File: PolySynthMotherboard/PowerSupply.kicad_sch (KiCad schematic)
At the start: 44 parts, among them J502 BATTERY, J503 POWER, Q501 Q_PMOS_GSD, Q502 Q_PMOS_GSD, U501 MAX1898, U502 TPS61200DRC, U503 CS5173, U702 TC7662Bx0A, U705 TC7662Bx0A

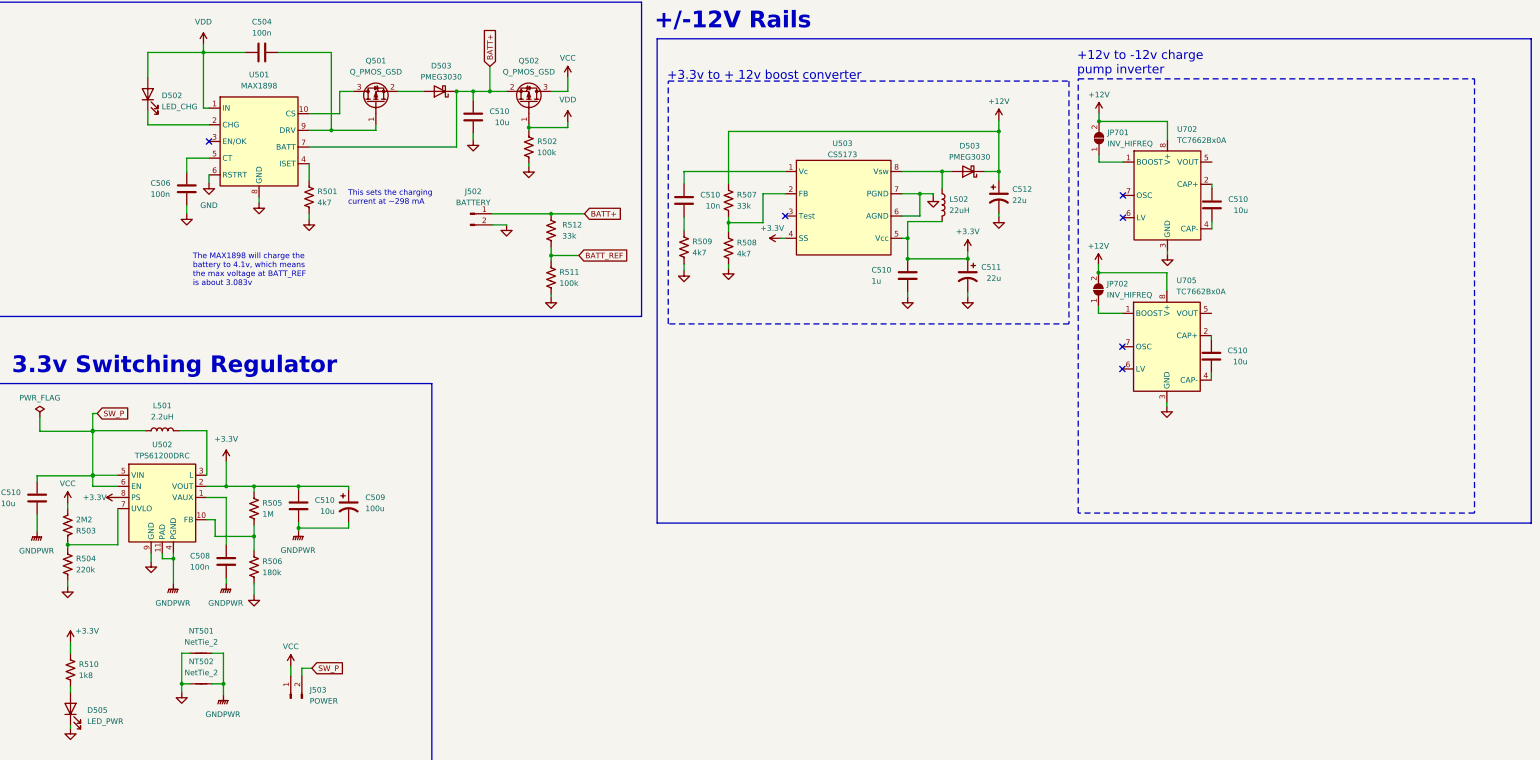
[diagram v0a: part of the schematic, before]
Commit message: net class assignment
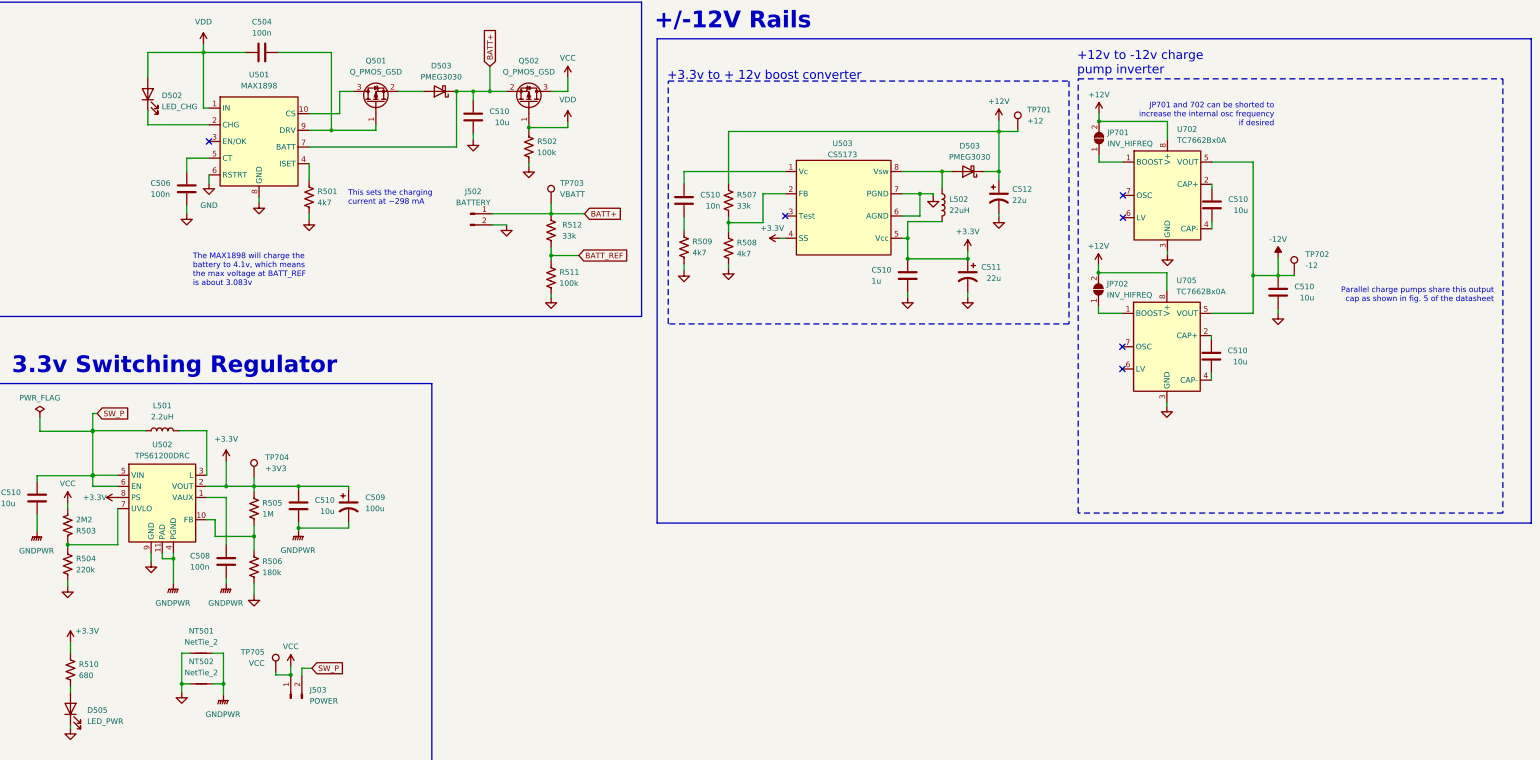
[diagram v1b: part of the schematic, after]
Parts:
- added C510: 10u, Capacitor_SMD:C_0805_2012Metric, symbol Device:C
- added TP701: +12, TestPoint:TestPoint_Pad_D1.0mm_Value, symbol Connector:TestPoint
- added TP702: -12, TestPoint:TestPoint_Pad_D1.0mm_Value, symbol Connector:TestPoint
- added TP703: VBATT, TestPoint:TestPoint_Pad_D1.0mm_Value, symbol Connector:TestPoint
- added TP704: +3V3, TestPoint:TestPoint_Pad_D1.0mm_Value, symbol Connector:TestPoint
- added TP705: VCC, TestPoint:TestPoint_Pad_D1.0mm_Value, symbol Connector:TestPoint
- JP701, JP702: footprint (none) -> Jumper:SolderJumper-2_Open_TrianglePad_0805
- R510: value 1k8 -> 680
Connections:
- net +12V: now also TP701.1
- net +3.3V: now also TP704.1
- net BATT+: now also TP703.1
- net GND: now also C510.2
- net VCC: now also TP705.1
- net -12V: now reaches U705.5 (VOUT)
- net -12V: now also U702.5 (VOUT), C510.1, TP702.1
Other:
- note added: "JP701 and 702 can be shorted to increase the internal osc frequency if desired"
- note added: "Parallel charge pumps share this output cap as shown in fig. 5 of the datasheet"

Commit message: board layout
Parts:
- U503: footprint PCM_4ms_Package_SOIC:SOIC-8_5.28x4.9mm_Pitch1.27mm -> Package_SO:SOIC-8_3.9x4.9mm_P1.27mm
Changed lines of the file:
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@@
       (effects (font (size 1.27 1.27)))
     )
-    (property "Footprint" "PCM_4ms_Package_SOIC:SOIC-8_5.28x4.9mm_Pitch1.27mm" (at 216.535 86.106 0)
+    (property "Footprint" "Package_SO:SOIC-8_3.9x4.9mm_P1.27mm" (at 216.535 86.106 0)
       (effects (font (size 1.27 1.27)) hide)
     )

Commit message: new voice board proj
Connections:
- net BATT_REF renamed BATT_LEF
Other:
- note added: "The MAX1898 will charge the battery to 4.1v, which means the max voltage at BATT_LEF is about 3.083v"
- note removed: "The MAX1898 will charge the battery to 4.1v, which means the max voltage at BATT_REF is about 3.083v"
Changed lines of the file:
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@@
     (effects (font (size 3.81 3.81) (thickness 0.762) bold) (justify left bottom))
   )
-  (text "The MAX1898 will charge the\nbattery to 4.1v, which means \nthe max voltage at BATT_REF \nis about 3.083v"
+  (text "The MAX1898 will charge the\nbattery to 4.1v, which means \nthe max voltage at BATT_LEF \nis about 3.083v"
     (at 69.85 104.8004 0)
     (effects (font (size 1.27 1.27)) (justify left bottom))
@@
     )
   )
-  (global_label "BATT_REF" (shape input) (at 157.988 97.663 0) (fields_autoplaced)
+  (global_label "BATT_LEF" (shape input) (at 157.988 97.663 0) (fields_autoplaced)
     (effects (font (size 1.27 1.27)) (justify left))
     (property "Intersheetrefs" "${INTERSHEET_REFS}" (at 169.7422 97.663 0)

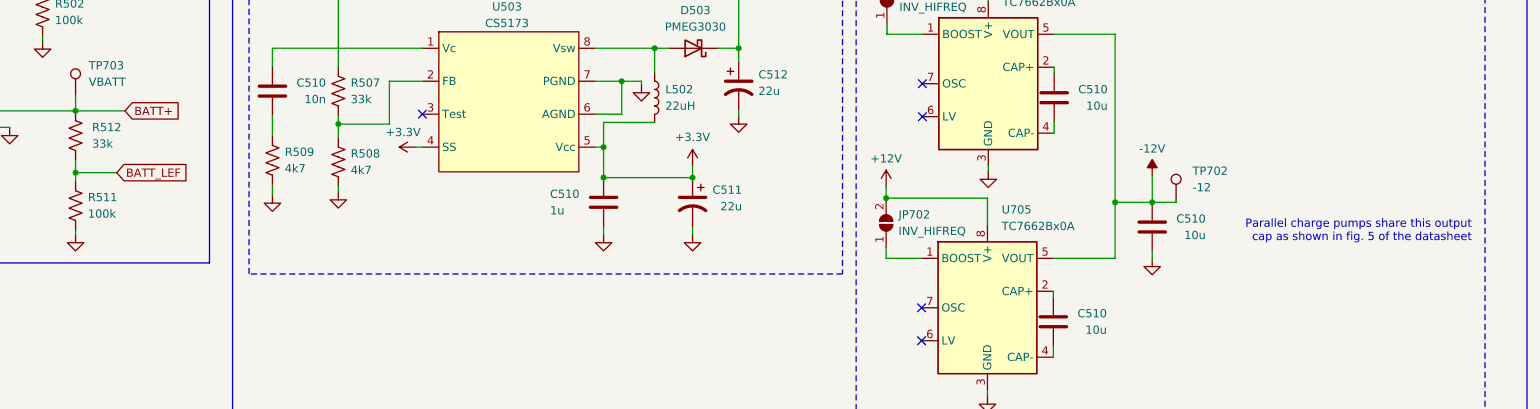
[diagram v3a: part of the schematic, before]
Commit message: op-amp layout improved
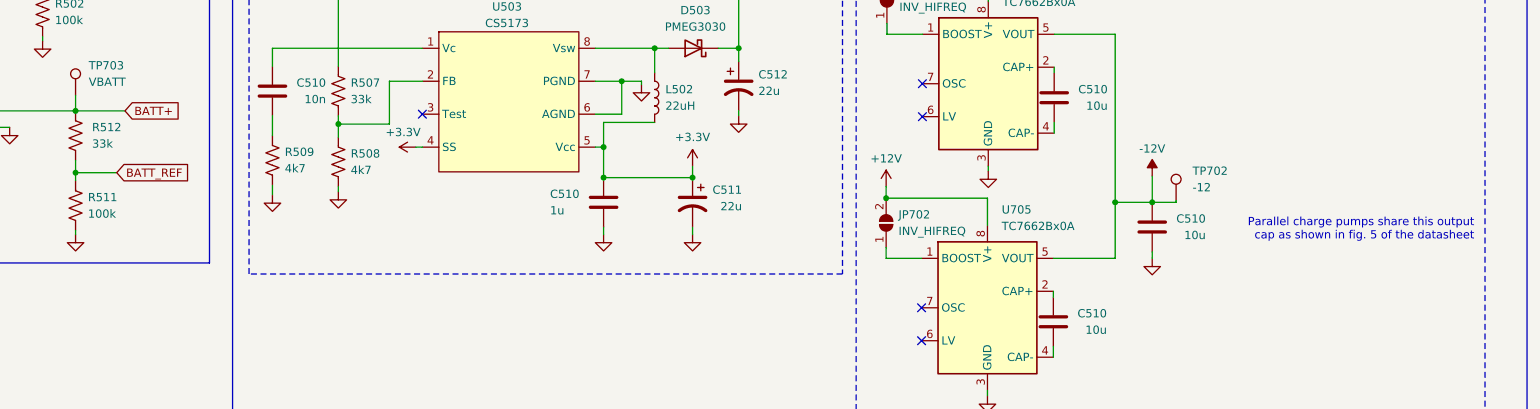
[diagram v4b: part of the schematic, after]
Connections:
- net BATT_LEF renamed BATT_REF
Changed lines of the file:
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@@
   )
   (text "Parallel charge pumps share this output\ncap as shown in fig. 5 of the datasheet"
-    (at 366.903 108.458 0)
+    (at 367.284 108.204 0)
     (effects (font (size 1.27 1.27)) (justify right bottom))
   )
@@
     )
   )
-  (global_label "BATT_LEF" (shape input) (at 157.988 97.663 0) (fields_autoplaced)
+  (global_label "BATT_REF" (shape input) (at 157.988 97.663 0) (fields_autoplaced)
     (effects (font (size 1.27 1.27)) (justify left))
     (property "Intersheetrefs" "${INTERSHEET_REFS}" (at 169.7422 97.663 0)

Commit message: power supply tweaks
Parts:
- removed C504, C506: 100n, Capacitor_SMD:C_0805_2012Metric, symbol Device:C
- removed C510: 10u, Capacitor_SMD:C_0805_2012Metric, symbol Device:C
- removed D502: LED_CHG, LED_THT:LED_D3.0mm, symbol Device:LED
- removed D503: PMEG3030, PCM_Diode_SMD_AKL:D_SOD-123, symbol Device:D_Schottky
- removed D505: LED_PWR, LED_THT:LED_D3.0mm, symbol Device:LED
- removed Q501, Q502: Q_PMOS_GSD, PCM_4ms_Package_SOT:SOT-23, symbol Device:Q_PMOS_GSD
- removed R501: 4k7, PCM_Resistor_SMD_AKL:R_0805_2012Metric, symbol Device:R_US
- removed R502: 100k, PCM_Resistor_SMD_AKL:R_0805_2012Metric, symbol Device:R_US
- removed R510: 680, PCM_Resistor_SMD_AKL:R_0805_2012Metric, symbol Device:R_US
- removed U501: MAX1898, PCM_Package_SO_AKL:MSOP-10_3x3mm_P0.5mm, symbol Battery_Management:MAX1898
- added C706: 2u2, symbol Device:C
- added C707: 10u, symbol Device:C
- added C708: 1u, symbol Device:C
- added D503 (x2): PMEG3030, PCM_Diode_SMD_AKL:D_SOD-123, symbol Device:D_Schottky
- added D702: PWR, symbol Device:LED
- added D703: CHG, symbol Device:LED
- added Q701: BSH205G2A, Package_TO_SOT_SMD_AKL:SOT-23, symbol Device:Q_PMOS_GSD
- added R704: 3k3, symbol Device:R_US
- added R705, R713: 470, symbol Device:R_US
- added R714: 10k, symbol Device:R_US
- added TH701: 10k, Resistor_SMD:R_0603_1608Metric, symbol Device:Thermistor_US
- added U703: MCP73834T, symbol Battery_Management:MCP73834T
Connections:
- net +3.3V: now also R705.1, R713.1, U703.7 (TE)
- net GND: now also C706.2, C707.2, C708.2, R704.2, R714.2, TH701.2, U703.5 (VSS)
- net VCC: now also C708.1, D503.1 (K), D503.1 (K)
- net VDD: now also C706.1, D503.2 (A), Q701.1 (G), R714.1, U703.1 (VDD), U703.2 (VDD)
- net BATT+ renamed VBATT
- net VBATT: now also C707.1, Q701.2 (S), U703.10 (VBATT), U703.9 (VBATT)
- new net: R704.1, U703.6 (PROG)
- new net: D702.2 (A), R713.2
- new net: D503.2 (A), Q701.3 (D)
- new net: D703.1 (K), U703.3 (STAT1)
- new net: D702.1 (K), U703.4 (STAT2)
- new net: TH701.1, U703.8 (THERM)
- new net: D703.2 (A), R705.2
- no-connect marks 6 -> 5
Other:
- note added: "Parallel charge pumps share output cap C713 as shown in fig. 5 of the datasheet"
- note added: "R704 sets the constant charging current at ~300mA (p. 14 of the datasheet)"
- note added: "This switches U704's input between the battery and the USB connector as appropriate"
- note removed: "Parallel charge pumps share this output cap as shown in fig. 5 of the datasheet"
- note removed: "The MAX1898 will charge the battery to 4.1v, which means the max voltage at BATT_LEF is about 3.083v"
- note removed: "This sets the charging current at ~298 mA"
- moved on the sheet: C508, C509, C510, J502, J503, JP701, JP702, L501, NT501, NT502, R503, R504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

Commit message: fixed git maybe
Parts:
- removed C508: 100n, Capacitor_SMD:C_0805_2012Metric, symbol Device:C
- removed C509: 100u, Capacitor_THT:CP_Radial_D5.0mm_P2.00mm, symbol Device:C_Polarized_US
- removed C510 (x2): 10u, Capacitor_SMD:C_0805_2012Metric, symbol Device:C
- removed J503: POWER, Connector_PinHeader_2.54mm:PinHeader_1x02_P2.54mm_Vertical, symbol Connector:Conn_01x02_Pin
- removed L501: 2.2uH, Inductor_SMD:L_Changjiang_FNR4010S, symbol Device:L
- removed NT501, NT502: NetTie_2, NetTie:NetTie-2_SMD_Pad0.5mm, symbol Device:NetTie_2
- removed R503: 2M2, PCM_Resistor_SMD_AKL:R_0805_2012Metric, symbol Device:R_US
- removed R504: 220k, PCM_Resistor_SMD_AKL:R_0805_2012Metric, symbol Device:R_US
- removed R505: 1M, PCM_Resistor_SMD_AKL:R_0805_2012Metric, symbol Device:R_US
- removed R506: 180k, PCM_Resistor_SMD_AKL:R_0805_2012Metric, symbol Device:R_US
- removed TP704: +3V3, TestPoint:TestPoint_Pad_D1.0mm_Value, symbol Connector:TestPoint
- removed TP705: VCC, TestPoint:TestPoint_Pad_D1.0mm_Value, symbol Connector:TestPoint
- removed U502: TPS61200DRC, Package_SON:VSON-10-1EP_3x3mm_P0.5mm_EP1.2x2mm, symbol Regulator_Switching:TPS61200DRC
- added C510 (x2): 1u, Capacitor_SMD:C_0805_2012Metric, symbol Device:C
- added C510, C712: 22u, Capacitor_SMD:C_0805_2012Metric, symbol Device:C
- added C510 (x3), C711: 100n, Capacitor_SMD:C_0805_2012Metric, symbol Device:C
- added C709, C710: 10u, Capacitor_SMD:C_0805_2012Metric, symbol Device:C
- added D704: LED, LED_SMD:LED_0805_2012Metric, symbol Device:LED
- added J502: POWER, Connector_PinHeader_2.54mm:PinHeader_1x02_P2.54mm_Vertical, symbol Connector:Conn_01x02_Pin
- added JP703: POS_CM, Jumper:SolderJumper-2_Open_TrianglePad_0805, symbol Jumper:SolderJumper_2_Open
- added JP704: NEG_CM, Jumper:SolderJumper-2_Open_TrianglePad_0805, symbol Jumper:SolderJumper_2_Open
- added JP705: DIG_CM, Jumper:SolderJumper-2_Open_TrianglePad_0805, symbol Jumper:SolderJumper_2_Open
- added L702: 1u5, Inductor_SMD:L_Coilcraft_XAL4020-XXX, symbol Device:L
- added Q702, Q703, Q704: TD6790, PCM_4ms_Package_SOIC:SM-8, symbol Transistor_BJT:TD6790
- added R511: 680, PCM_Resistor_SMD_AKL:R_0805_2012Metric, symbol Device:R_US
- added R709, R710, R715: 12k, PCM_Resistor_SMD_AKL:R_0805_2012Metric, symbol Device:R_US
- added U704: TPS63021, Package_SON:Texas_S-PVSON-N14, symbol Regulator_Switching:TPS63021
- C706, C707, C708: footprint (none) -> Capacitor_SMD:C_0805_2012Metric
- D702, D703: footprint (none) -> LED_THT:LED_D3.0mm
- Q701: footprint Package_TO_SOT_SMD_AKL:SOT-23 -> PCM_4ms_Package_SOT:SOT-23
- R704, R705, R713, R714: footprint (none) -> PCM_Resistor_SMD_AKL:R_0805_2012Metric
- TP701: value +12 -> +12A
- TP702: value -12 -> -12A
- U703: footprint (none) -> PCM_Package_SO_AKL:MSOP-10_3x3mm_P0.5mm
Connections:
- net +12V: now also C510.1, JP703.1 (A), Q703.3 (C2), Q703.7 (E1); no longer C512.1, D503.1 (K), R507.1, TP701.1
- net +3.3V: now also C510.1, JP705.1 (A), Q704.3 (C2), Q704.7 (E1)
- net -12V: now also C510.1, JP704.1 (A), Q702.1 (C1), Q702.5 (E2); no longer C510.1, TP702.1, U702.5 (VOUT), U705.5 (VOUT)
- net GND: now also C510.2, C510.2, C510.2, C510.2, C510.2, C510.2, C709.2, C710.2, C711.2, C712.2, U704.15 (PGND), U704.2 (GND)
- net VCC: now also J502.1 (Pin_1)
- new net: Q702.3 (C2), Q702.8 (B1)
- new net: C510.1, Q702.6 (B2), R715.2
- new net: Q704.1 (C1), Q704.6 (B2)
- new net: C510.1, Q704.8 (B1), R709.2
- new net: D704.2 (A), R511.2
- new net: C510.1, Q703.8 (B1), R710.2
- new net: Q703.1 (C1), Q703.6 (B2)
- new net: L702.1, U704.8 (L1)
- new net: L702.2, U704.6 (L2)
- new net: D704.1 (K), U704.14 (PG)
- new net +12VA: C512.1, D503.1 (K), JP703.2 (B), Q703.5 (E2), R507.1, R710.1, TP701.1
- new net +3.3VP: C712.1, JP705.2 (B), Q704.5 (E2), R511.1, R709.1, U704. (FB), U704.4 (VOUT)
- new net -12VA: C510.1, JP704.2 (B), Q702.7 (E1), R715.1, TP702.1, U702.5 (VOUT), U705.5 (VOUT)
- new net VIN: U704.11 (VIN)
- new net V_PWR: C709.1, C710.1, C711.1, J502.2 (Pin_2), U704.1 (VINA), U704.10 (VIN), U704.12 (EN), U704.13 (PSSYNC)
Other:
- note added: "BJT capacitance multipliers"
- note added: "These capacitance multipliers should smooth the power lines to <1mV of ripple when populated, if not they can be bypassed with solder jumpers"
- moved on the sheet: C510, C511, C512, D503, J502, JP701, JP702, L502, R507, R508, R509, R511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

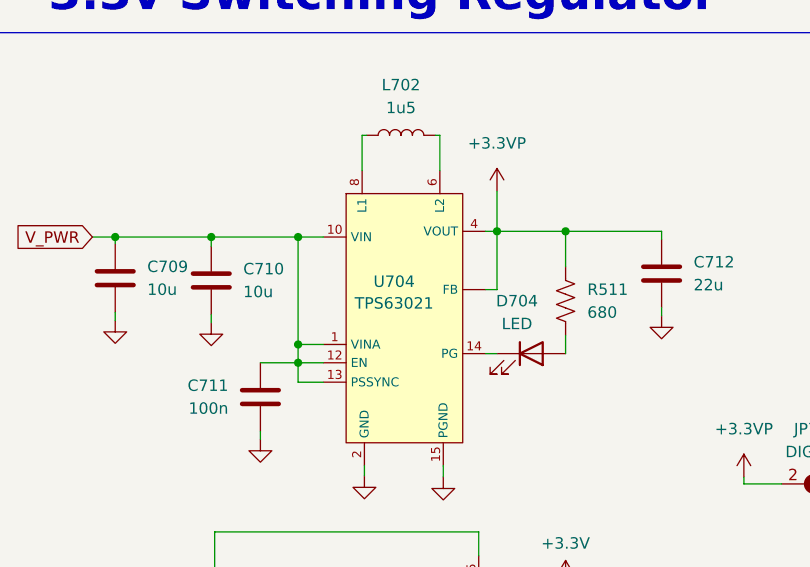
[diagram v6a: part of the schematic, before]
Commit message: cleaned up CV opamps
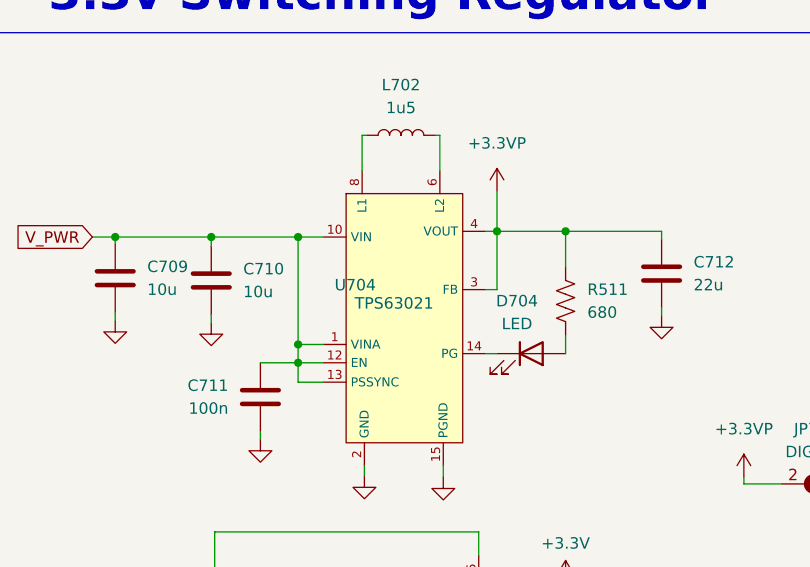
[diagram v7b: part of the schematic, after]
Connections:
- net +3.3VP: now also U704.3 (FB); no longer U704. (FB)
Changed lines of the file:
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@@
   (symbol (lib_id "Regulator_Switching:TPS63021") (at 68.834 213.233 0) (unit 1)
     (in_bom yes) (on_board yes) (dnp no)
-    (property "Reference" "U704" (at 64.77 209.296 0)
+    (property "Reference" "U704" (at 60.452 209.677 0)
       (effects (font (size 1.27 1.27)))
     )
@@
       (effects (font (size 1.27 1.27)) hide)
     )
-    (pin "")
     (pin "1")
     (pin "10")
@@
     (pin "15")
     (pin "2")
+    (pin "3")
     (pin "4")
     (pin "5")
